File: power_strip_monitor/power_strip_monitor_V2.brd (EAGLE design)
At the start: 185 x 95 mm, 71 parts, among them IC2 ATMEGA644A, J1 EXP, Q1 16.384MHz, Q2 BTA312B-800E, Q3 BTA312B-800E, Q4 BTA312B-800E, Q5 BTA312B-800E, Q6 BTA312B-800E, Q7 BTA312B-800E, U1 CS5467, U10 LTP5901, U2 CS5467, U3 CS5467, U5 RAC01_02-SC, U8 SN74LVC4245A, U9 SN74LVC4245A

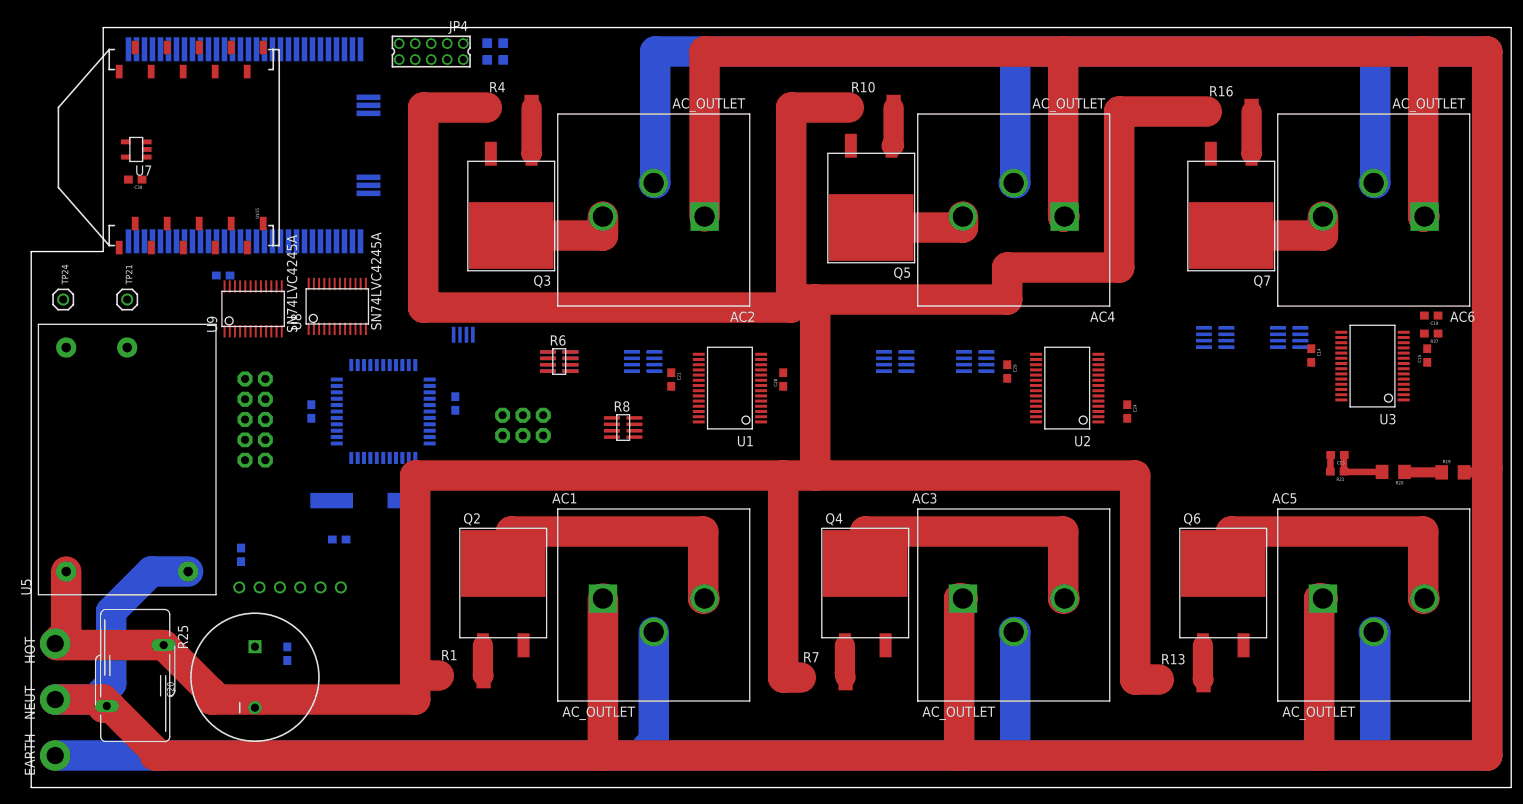
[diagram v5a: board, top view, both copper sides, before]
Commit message: ready for mfg? BOM needs fixing
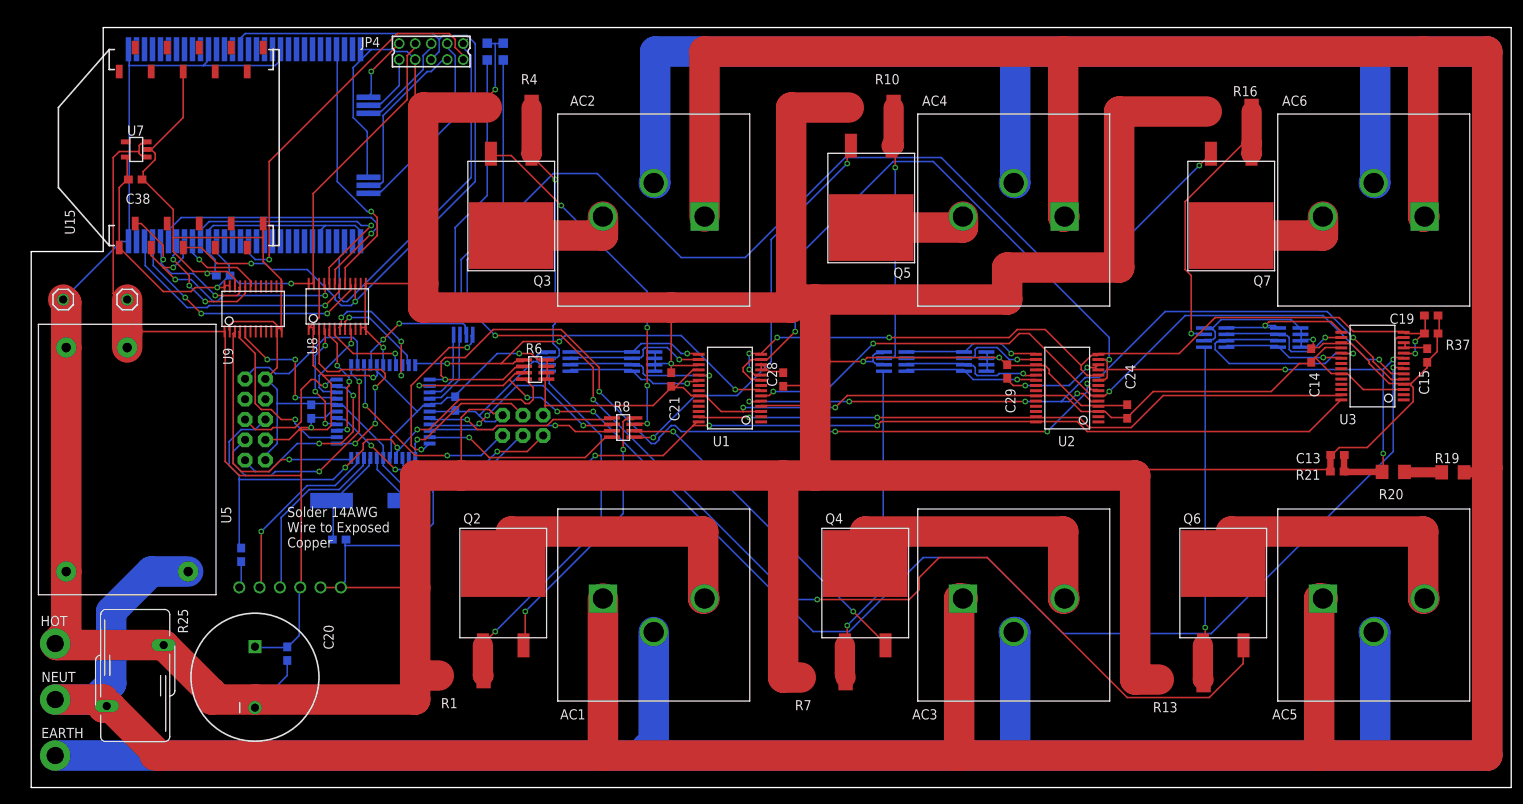
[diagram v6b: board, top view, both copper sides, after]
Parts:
- C1, C2, C3: value CAP_ARRAY -> 10n
- R6: value (none) -> 10k
- U7: value (none) -> LT1761ES5-3.3
- moved R6 3.16 mm to (63.0, 52.2)
- renumbered J1 to EXP, JP1 to FTDI, JP2 to JTAG, U$15 to U15
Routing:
- net GND: track 445.5 -> 991.2 mm, vias 0 -> 7
- net 5V: track 0.00 -> 318.6 mm, vias 0 -> 5
- net #CS3: track 0.00 -> 167.7 mm, vias 0 -> 5
- net V+: track 6.85 -> 142.4 mm, vias 0 -> 5
- net XIN: track 0.00 -> 134.5 mm, vias 0 -> 5
- net GATE5: track 0.00 -> 127.9 mm, vias 0 -> 3
- net GATE6: track 0.00 -> 124.1 mm, vias 0 -> 1
- net #CS2: track 0.00 -> 111.4 mm, vias 0 -> 5
- net V-: track 0.00 -> 104.5 mm, vias 0 -> 6
- net MOTE_RESETN_3V: track 0.00 -> 100.3 mm, vias 0 -> 2
- net SCLK: track 0.00 -> 97.3 mm, vias 0 -> 5
- net MISO: track 0.00 -> 94.1 mm, vias 0 -> 4
- net MOSI: track 0.00 -> 82.7 mm, vias 0 -> 2
- net 3.3V: track 0.00 -> 82.2 mm, vias 0 -> 2
- net RST: track 0.00 -> 67.0 mm, vias 0 -> 3
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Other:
- board text added: "Do not plug into computer while connected to mains!"
- board text added: "Power Strip Monitor Kevin Weekly"
- board text added: "SinBerBEST Project UC Berkeley"
- board text added: "Solder 14AWG Wire to Exposed Copper"
- board text removed: "SOLDER 14AWG WIRE ON BUS"
